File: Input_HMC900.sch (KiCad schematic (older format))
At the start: 6 parts

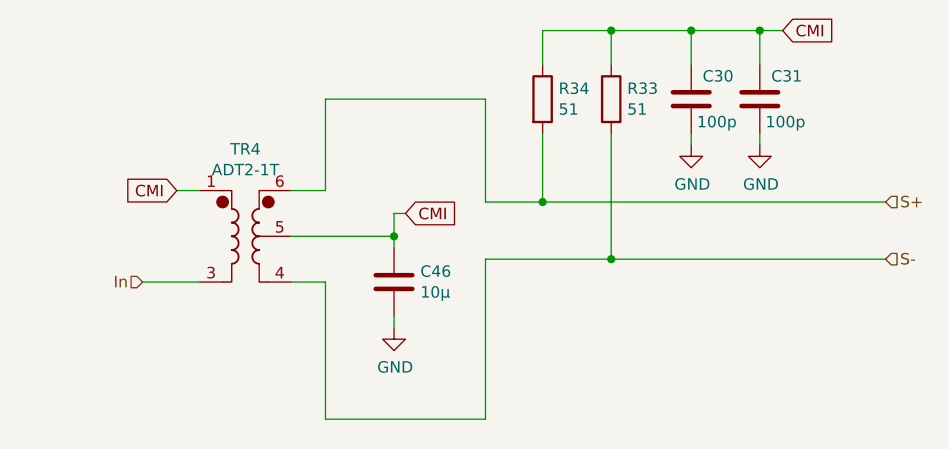
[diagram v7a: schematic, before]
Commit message: Added options for the tranfo
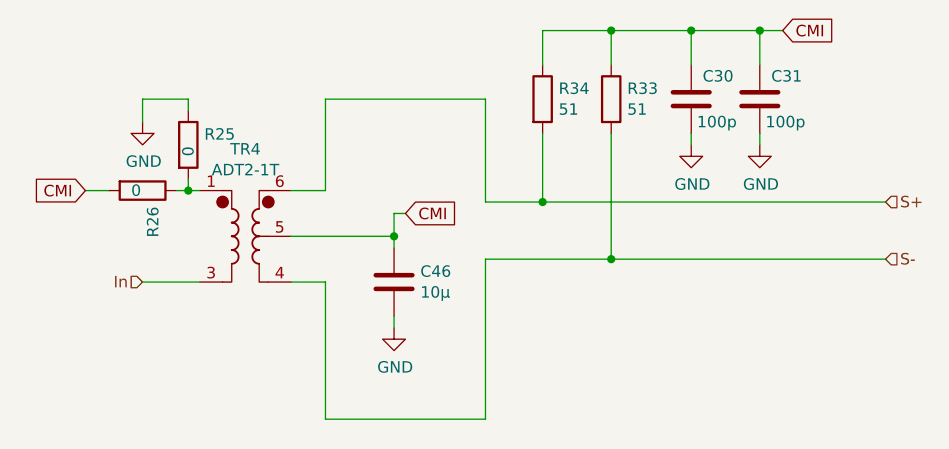
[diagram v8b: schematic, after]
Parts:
- added R22, R23: 0, Resistor_SMD:R_0603_1608Metric_Pad0.98x0.95mm_HandSolder, symbol Device:R
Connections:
- net CMI: now also R23.2; no longer TR4.1
- net GND: now also R22.1
- new net: R22.2, R23.1, TR4.1
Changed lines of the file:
@@
 $Descr A4 11693 8268
 encoding utf-8
-Sheet 5 7
+Sheet 4 7
 Title ""
 Date ""
@@
 	4900 3500 4900 3550
 Wire Wire Line
-	4050 3300 3950 3300
+	4050 3300 4000 3300
 $Comp
 L Device:C C?
@@
 Wire Wire Line
 	4600 4300 5300 4300
-Text GLabel 3950 3300 0    50   Input ~ 0
+Text GLabel 3550 3300 0    50   Input ~ 0
 CMI
+$Comp
+L Device:R R?
+U 1 1 614655FD
+P 3800 3300
+AR Path="/60D21B6E/614655FD" Ref="R?"  Part="1"
+AR Path="/60D21B6E/60D894BC/614655FD" Ref="R?"  Part="1"
+AR Path="/60D21B6E/6110419F/614655FD" Ref="R?"  Part="1"
+AR Path="/60D21B6E/61121120/614655FD" Ref="R23"  Part="1"
+AR Path="/60D21B6E/60F52DEE/614655FD" Ref="R26"  Part="1"
+F 0 "R26" H 3870 3346 50  0000 L CNN
+F 1 "0" V 3800 3250 50  0000 L CNN
+F 2 "Resistor_SMD:R_0603_1608Metric_Pad0.98x0.95mm_HandSolder" V 3730 3300 50  0001 C CNN
+F 3 "~" H 3800 3300 50  0001 C CNN
+	1    3800 3300
+	0    1    1    0
+$EndComp
+Wire Wire Line
+	3650 3300 3550 3300
+$Comp
+L Device:R R?
+U 1 1 6147240B
+P 4000 3100
+AR Path="/60D21B6E/6147240B" Ref="R?"  Part="1"
+AR Path="/60D21B6E/60D894BC/6147240B" Ref="R?"  Part="1"
+AR Path="/60D21B6E/6110419F/6147240B" Ref="R?"  Part="1"
+AR Path="/60D21B6E/61121120/6147240B" Ref="R22"  Part="1"
+AR Path="/60D21B6E/60F52DEE/6147240B" Ref="R25"  Part="1"
+F 0 "R25" H 4070 3146 50  0000 L CNN
+F 1 "0" V 4000 3050 50  0000 L CNN
+F 2 "Resistor_SMD:R_0603_1608Metric_Pad0.98x0.95mm_HandSolder" V 3930 3100 50  0001 C CNN
+F 3 "~" H 4000 3100 50  0001 C CNN
+	1    4000 3100
+	1    0    0    -1
+$EndComp
+$Comp
+L power:GND #PWR?
+U 1 1 614747AB
+P 3800 3000
+AR Path="/60D21B6E/614747AB" Ref="#PWR?"  Part="1"
+AR Path="/60D21B6E/60D894BC/614747AB" Ref="#PWR?"  Part="1"
+AR Path="/60D21B6E/6110419F/614747AB" Ref="#PWR?"  Part="1"
+AR Path="/60D21B6E/61121120/614747AB" Ref="#PWR09"  Part="1"
+AR Path="/60D21B6E/60F52DEE/614747AB" Ref="#PWR010"  Part="1"
+F 0 "#PWR010" H 3800 2750 50  0001 C CNN
+F 1 "GND" H 3805 2827 50  0000 C CNN
+F 2 "" H 3800 3000 50  0001 C CNN
+F 3 "" H 3800 3000 50  0001 C CNN
+	1    3800 3000
+	1    0    0    -1
+$EndComp
+Wire Wire Line
+	3800 2900 4000 2900
+Wire Wire Line
+	4000 2900 4000 2950
+Wire Wire Line
+	3800 2900 3800 3000
+Wire Wire Line
+	4000 3250 4000 3300
+Connection ~ 4000 3300
+Wire Wire Line
+	4000 3300 3950 3300
 $EndSCHEMATC
